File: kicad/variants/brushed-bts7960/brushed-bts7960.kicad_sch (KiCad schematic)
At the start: 57 parts, among them IC1 rp2040_RP2040_breakout_swd, J1 HDR-M-2.54_1x3, J2 HDR-M-2.54_1x4, J3 HDR-M-2.54_1x4, J4 HDR-M-2.54_1x4, U1 SN74AHC244DW, U2 BTN7970, U3 BTN7970, U4 BTN7970, U5 BTN7970, U6 BMI160, U7 SPX3819M5-L-3-3/TR

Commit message: feat(kicad): convert EasyEDA schematic to KiCad preserving wires and layout
- scripts/easyeda_sch2kicad.py: EasyEDA RP2040.json -> .kicad_sch with original component positions, wires, net labels, junctions, no-connect markers
- biba.kicad_sym: symbols regenerated from EasyEDA pin layouts (18 unique)
- ERC: 0 unconnected pins; 12 dangling wire stubs (EasyEDA polyline quirks)
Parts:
- removed C2, C3, C6: 0.1u, symbol biba:C
- removed C7: 1uF, symbol biba:C
- removed C8: 2.2uF, symbol biba:C
- removed C9: 1000uF, symbol biba:C
- removed H1, H10, H2, H3, H4, H5, H6, H7, H8: HDR-F-2.54_1x3, symbol biba:CONN_1X3
- removed IC1: rp2040_RP2040_breakout_swd, symbol biba:RP2040
- removed J1: HDR-M-2.54_1x3, symbol biba:CONN_1X3
- removed J2, J3, J4: HDR-M-2.54_1x4, symbol biba:CONN_1X4
- removed PM1: SKMW30f-05, symbol biba:SKMW30G
- removed R13, R14, R15, R16, R21, R22, R23, R24: 10k, symbol biba:R
- removed R17, R18, R19, R20, R25, R26: 1k, symbol biba:R
- removed U1: SN74AHC244DW, symbol biba:SN74AHC244
- removed U2, U3, U4, U5: BTN7970, symbol biba:BTN7970
- removed U6: BMI160, symbol biba:BMI160
- removed U7: SPX3819M5-L-3-3/TR, symbol biba:SPX3819
- added C2, C3: 0.1u, symbol biba:C_1
- added C6: 0.1u, symbol biba:C_2
- added C7: 1uF, symbol biba:C_1
- added C8: 2.2uF, symbol biba:C_2
- added C9: 1000uF, symbol biba:C_3
- added H1, H2, H3, H4, H5, H6, H7, H8: HDR-F-2.54_1x3, symbol biba:H
- added H10: HDR-F-2.54_1x3, symbol biba:H_1
- added IC1: rp2040_RP2040_breakout_swd, symbol biba:IC
- added J1: HDR-M-2.54_1x3, symbol biba:J
- added J2, J3, J4: HDR-M-2.54_1x4, symbol biba:J_1
- added PM1: SKMW30f-05, symbol biba:PM
- added R13, R16, R21, R22, R23, R24: 10k, symbol biba:R_1
- added R14, R15: 10k, symbol biba:R_2
- added R17, R18, R19, R20, R25, R26: 1k, symbol biba:R_1
- added U1: SN74AHC244DW, symbol biba:U
- added U2, U4: BTN7970, symbol biba:U_1
- added U3, U5: BTN7970, symbol biba:U_2
- added U6: BMI160, symbol biba:U_3
- added U7: SPX3819M5-L-3-3/TR, symbol biba:U_4
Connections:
- net +5V: now also C7.2, H1.2, H2.2, H3.2, H4.2, H5.2, H6.2, H7.2, H8.2, IC1.39, J1.3, J2.3, J3.1, J4.1, PM1.3, U1.20, U7.1, U7.3
- net 3.3V: now also C6.1, C8.1, R21.1, R22.2, R23.2, R24.2, U6.5, U6.8, U7.5
- net CRSF_RX: now also IC1.2, J3.4
- net CRSF_TX: now also IC1.1, J3.3
- net GND: now also C2.1, C3.1, C6.2, C7.1, C8.2, C9.2, H1.3, H10.1, H2.3, H3.3, H4.3, H5.3, H6.3, H7.3, H8.3, IC1.13, IC1.18, IC1.23, IC1.28, IC1.3, IC1.33, IC1.38, IC1.44, IC1.8, J1.1, J2.2, J2.4, J3.2, J4.2, PM1.2, PM1.5, R13.1, R14.2, R15.2, R16.1, R24.1, U1.1, U1.10, U1.19, U2.1, U3.1, U4.1, U5.1, U6.1, U6.6, U6.7, U7.2
- net GP10: now also H1.1, IC1.14
- net GP11: now also H2.1, IC1.15
- net GP14: now also H3.1, IC1.19
- net GP15: now also H4.1, IC1.20
- net GP16: now also H5.1, IC1.21
- net GP17: now also H6.1, IC1.22
- net GP18: now also H7.1, IC1.24
- net GP19: now also H8.1, IC1.25
- net I2C0_SCL: now also IC1.27, R22.1, U6.13
- net I2C0_SDA: now also IC1.26, R23.1, U6.14
- net IBAT: now also H10.3, R25.2
- net IMU_INT1: now also IC1.29, U6.4
- net IN1: now also U1.18, U2.2
- net IN2: now also U1.14, U3.2
- net IN3: now also U1.9, U4.2
- net IN4: now also U1.5, U5.2
- net INH1: now also U1.16, U2.3
- net INH2: now also U1.12, U3.3
- net INH3: now also U1.7, U4.3
- net INH4: now also U1.3, U5.3
- net L_IS: now also C3.2, IC1.32, R19.1, R20.1
- net L_LEN: now also IC1.7, U1.17
- net L_LPWM: now also IC1.5, U1.15
- net L_REN: now also IC1.6, U1.13
- net L_RPWM: now also IC1.4, U1.11
- net M1+: now also U2.4, U2.8
- net M1-: now also U3.4, U3.8
- net M2+: now also U4.4, U4.8
- net M2-: now also U5.4, U5.8
- net R_IS: now also C2.2, IC1.31, R17.1, R18.1
- net R_LEN: now also IC1.12, U1.8
- net R_LPWM: now also IC1.10, U1.6
- net R_REN: now also IC1.11, U1.4
- net R_RPWM: now also IC1.9, U1.2
- net SW: now also J2.1, PM1.6
- net UART1_RX: now also IC1.17, J4.4
- net UART1_TX: now also IC1.16, J4.3
- net VBAT: now also H10.2, R26.2
- net IC1_34: no longer names the net of C5.1
- net IC1_34: now also IC1.34, R26.1
- net IC1_35: no longer names the net of C4.1
- net IC1_35: now also IC1.35, R25.1
- net U2_5: no longer names the net of R12.2
- net U2_5: now also U2.5
- net U2_6: no longer names the net of R11.2
- net U2_6: now also R17.2, U2.6
- net U4_5: no longer names the net of R10.2
- net U4_5: now also U4.5
- net U4_6: no longer names the net of R9.2
- net U4_6: now also R19.2, U4.6
- new net: R13.2, R18.2, U3.6
- new net: R15.1, R20.2, U5.6
- new net: R21.2, U6.12
- new net: J1.2, PM1.4
- new net: R16.2, U5.5
- new net: R14.1, U3.5
- new net Vin: C9.1, PM1.1, U2.7, U3.7, U4.7, U5.7

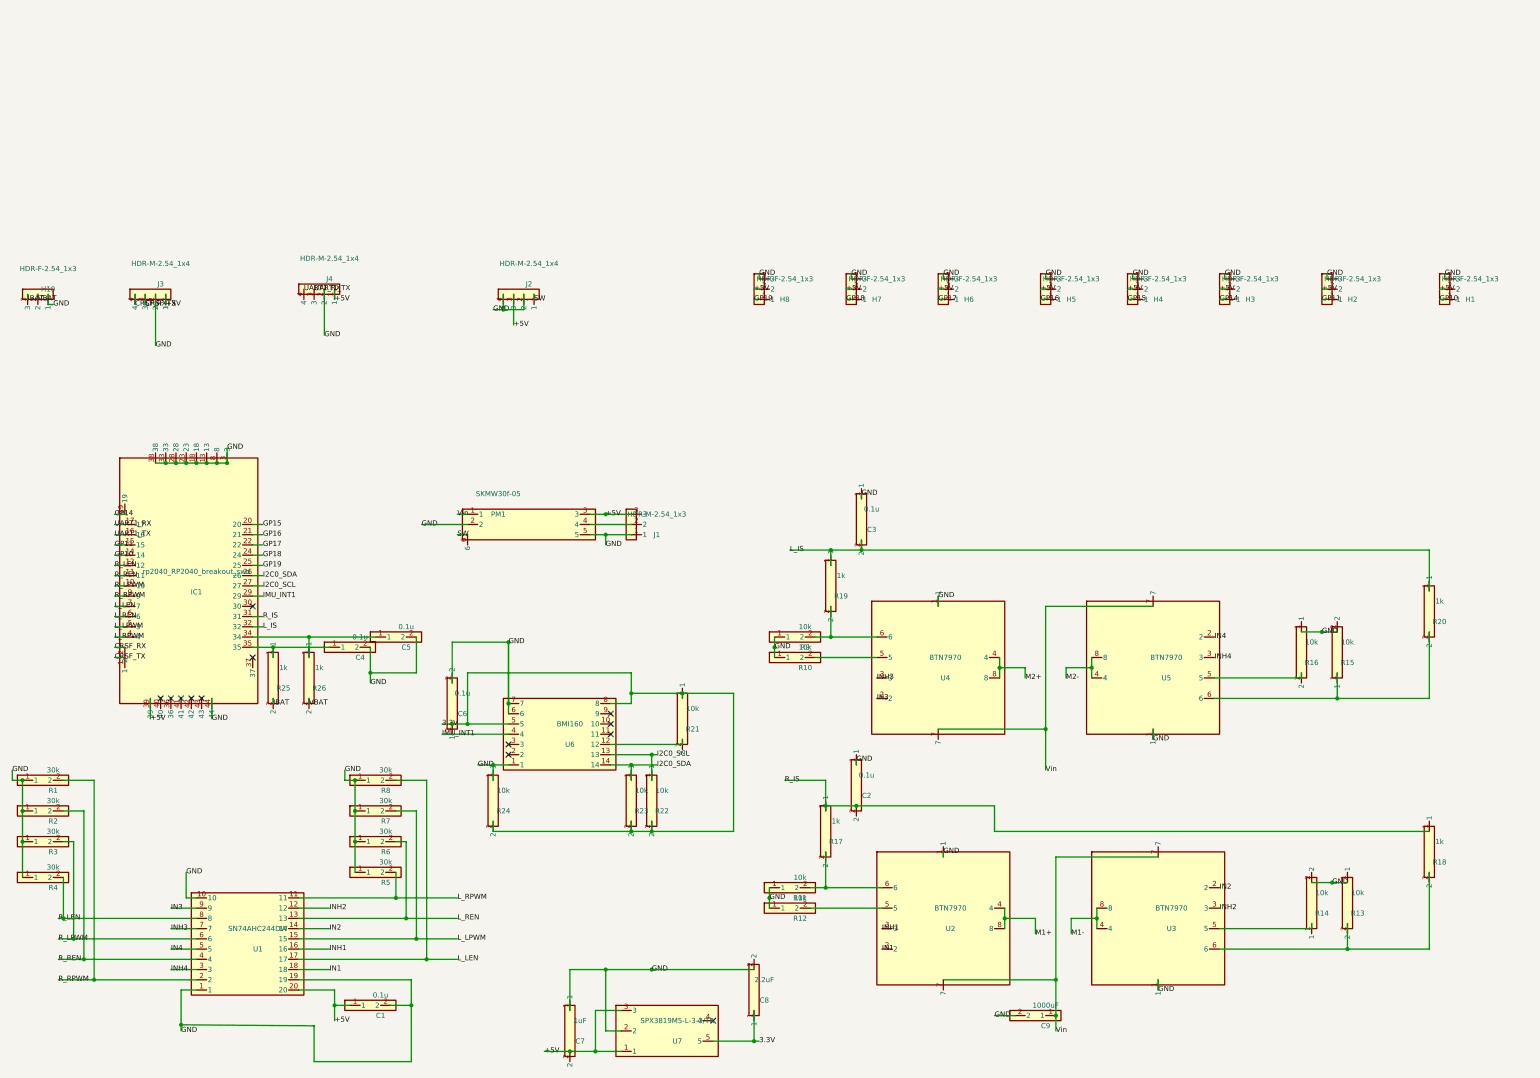
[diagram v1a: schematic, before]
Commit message: feat(kicad): preserve full EasyEDA symbol graphics and pin geometry
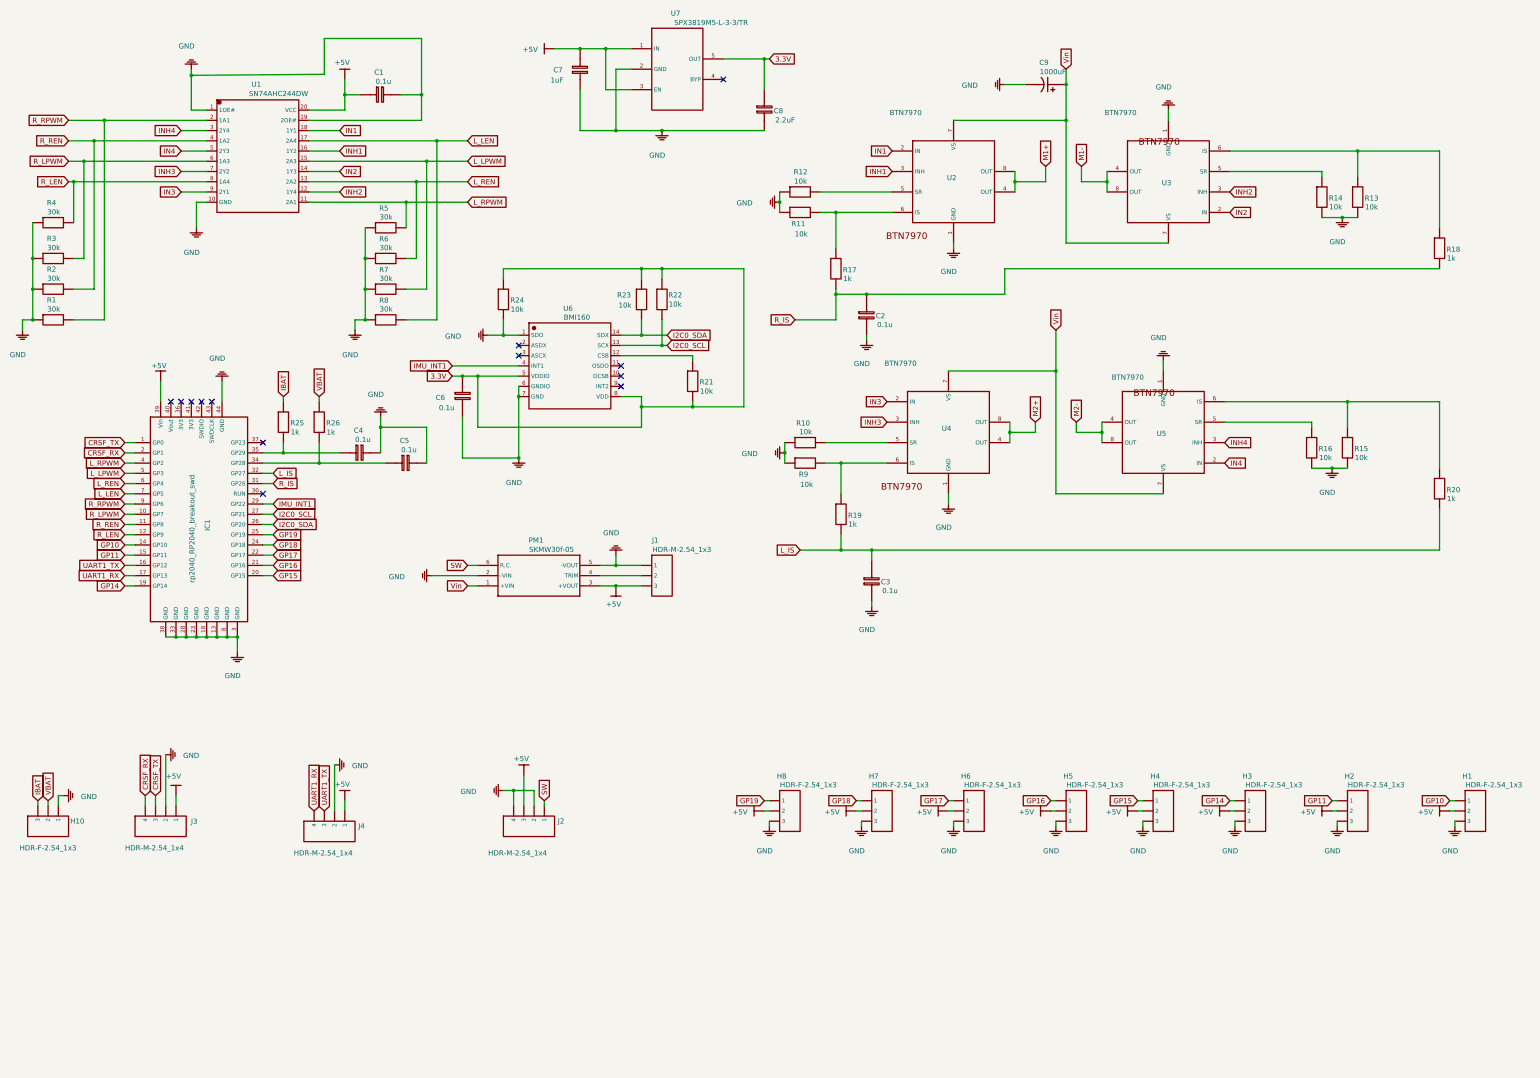
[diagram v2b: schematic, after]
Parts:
- removed C9: 1000uF, symbol biba:C_3
- removed H1, H2, H3, H4, H5, H6, H7, H8: HDR-F-2.54_1x3, symbol biba:H
- removed H10: HDR-F-2.54_1x3, symbol biba:H_1
- removed IC1: rp2040_RP2040_breakout_swd, symbol biba:IC
- removed J1: HDR-M-2.54_1x3, symbol biba:J
- removed J2, J3, J4: HDR-M-2.54_1x4, symbol biba:J_1
- removed PM1: SKMW30f-05, symbol biba:PM
- removed U1: SN74AHC244DW, symbol biba:U
- removed U2, U4: BTN7970, symbol biba:U_1
- removed U3, U5: BTN7970, symbol biba:U_2
- removed U6: BMI160, symbol biba:U_3
- removed U7: SPX3819M5-L-3-3/TR, symbol biba:U_4
- added C9: 1000uF, symbol biba:C_Pol
- added H1, H2, H3, H4, H5, H6, H7, H8: HDR-F-2.54_1x3, symbol biba:HDR-F-2.54_1x3
- added H10: HDR-F-2.54_1x3, symbol biba:HDR-F-2.54_1x3_1
- added IC1: rp2040_RP2040_breakout_swd, symbol biba:rp2040_RP2040_breakout_swd
- added J1: HDR-M-2.54_1x3, symbol biba:HDR-M-2.54_1x3
- added J2, J3, J4: HDR-M-2.54_1x4, symbol biba:HDR-M-2.54_1x4
- added PM1: SKMW30f-05, symbol biba:SKMW30f-05
- added U1: SN74AHC244DW, symbol biba:SN74AHC244DW
- added U2, U4: BTN7970, symbol biba:BTN7970
- added U3: BTN7970, symbol biba:BTN7970_1
- added U5: BTN7970, symbol biba:BTN7970_2
- added U6: BMI160, symbol biba:BMI160
- added U7: SPX3819M5-L-3-3/TR, symbol biba:SPX3819M5-L-3-3_TR
- C1, C2, C3, C4, C5, C6: Package (none) -> C0805
- C7, C8: Package (none) -> C0603
- R1, R10, R11, R12, R13, R14, R15, R16, R17, R18, R19, R2, R20, R25, R26, R3, R4, R5, R6, R7, R8, R9: Package (none) -> R0805
- R21, R22, R23, R24: Package (none) -> R0603
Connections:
- net +5V: now also H1.2, H2.2, H3.2, H4.2, H5.2, H6.2, H7.2, H8.2, IC1.39 (Vin), J1.3, J2.3, J3.1, J4.1, PM1.3 (+VOUT), U1.20 (VCC), U7.1 (IN), U7.3 (EN)
- net 3.3V: now also U6.5 (VDDIO), U6.8 (VDD), U7.5 (OUT)
- net CRSF_RX: now also IC1.2 (GP1), J3.4
- net CRSF_TX: now also IC1.1 (GP0), J3.3
- net GND: now also C9.2, H1.3, H10.1, H2.3, H3.3, H4.3, H5.3, H6.3, H7.3, H8.3, IC1.13 (GND), IC1.18 (GND), IC1.23 (GND), IC1.28 (GND), IC1.3 (GND), IC1.33 (GND), IC1.38 (GND), IC1.44 (GND), IC1.8 (GND), J1.1, J2.2, J2.4, J3.2, J4.2, PM1.2 (-VIN), PM1.5 (-VOUT), U1.1 (1OE#), U1.10 (GND), U1.19 (2OE#), U2.1 (GND), U3.1 (GND), U4.1 (GND), U5.1 (GND), U6.1 (SDO), U6.6 (GNDIO), U6.7 (GND), U7.2 (GND)
- net GP10: now also H1.1, IC1.14 (GP10)
- net GP11: now also H2.1, IC1.15 (GP11)
- net GP14: now also H3.1, IC1.19 (GP14)
- net GP15: now also H4.1, IC1.20 (GP15)
- net GP16: now also H5.1, IC1.21 (GP16)
- net GP17: now also H6.1, IC1.22 (GP17)
- net GP18: now also H7.1, IC1.24 (GP18)
- net GP19: now also H8.1, IC1.25 (GP19)
- net I2C0_SCL: now also IC1.27 (GP21), U6.13 (SCX)
- net I2C0_SDA: now also IC1.26 (GP20), U6.14 (SDX)
- net IBAT: now also H10.3
- net IMU_INT1: now also IC1.29 (GP22), U6.4 (INT1)
- net IN1: now also U1.18 (1Y1), U2.2 (IN)
- net IN2: now also U1.14 (1Y3), U3.2 (IN)
- net IN3: now also U1.9 (2Y1), U4.2 (IN)
- net IN4: now also U1.5 (2Y3), U5.2 (IN)
- net INH1: now also U1.16 (1Y2), U2.3 (INH)
- net INH2: now also U1.12 (1Y4), U3.3 (INH)
- net INH3: now also U1.7 (2Y2), U4.3 (INH)
- net INH4: now also U1.3 (2Y4), U5.3 (INH)
- net L_IS: now also IC1.32 (GP27)
- net L_LEN: now also IC1.7 (GP5), U1.17 (2A4)
- net L_LPWM: now also IC1.5 (GP3), U1.15 (2A3)
- net L_REN: now also IC1.6 (GP4), U1.13 (2A2)
- net L_RPWM: now also IC1.4 (GP2), U1.11 (2A1)
- net M1+: now also U2.4 (OUT), U2.8 (OUT)
- net M1-: now also U3.4 (OUT), U3.8 (OUT)
- net M2+: now also U4.4 (OUT), U4.8 (OUT)
- net M2-: now also U5.4 (OUT), U5.8 (OUT)
- net R_IS: now also IC1.31 (GP26)
- net R_LEN: now also IC1.12 (GP9), U1.8 (1A4)
- net R_LPWM: now also IC1.10 (GP7), U1.6 (1A3)
- net R_REN: now also IC1.11 (GP8), U1.4 (1A2)
- net R_RPWM: now also IC1.9 (GP6), U1.2 (1A1)
- net SW: now also J2.1, PM1.6 (R.C.)
- net UART1_RX: now also IC1.17 (GP13), J4.4
- net UART1_TX: now also IC1.16 (GP12), J4.3
- net VBAT: now also H10.2
- net Vin: now also C9.1, PM1.1 (+VIN), U2.7 (VS), U3.7 (VS), U4.7 (VS), U5.7 (VS)
- net at C5.1, R26.1: now also IC1.34 (GP28)
- net at C4.1, R25.1: now also IC1.35 (GP29)
- net at R10.2: now also U4.5 (SR)
- net at R13.2, R18.2: now also U3.6 (IS)
- net at R15.1, R20.2: now also U5.6 (IS)
- net at R11.2, R17.2: now also U2.6 (IS)
- net at R21.2: now also U6.12 (CSB)
- net at R19.2, R9.2: now also U4.6 (IS)
- net at R12.2: now also U2.5 (SR)
- net at R16.2: now also U5.5 (SR)
- net at R14.1: now also U3.5 (SR)
- new net: J1.2, PM1.4 (TRIM)
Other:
- title: (none) -> BiBa — RP2040, 4× BTN7970 (brushed)

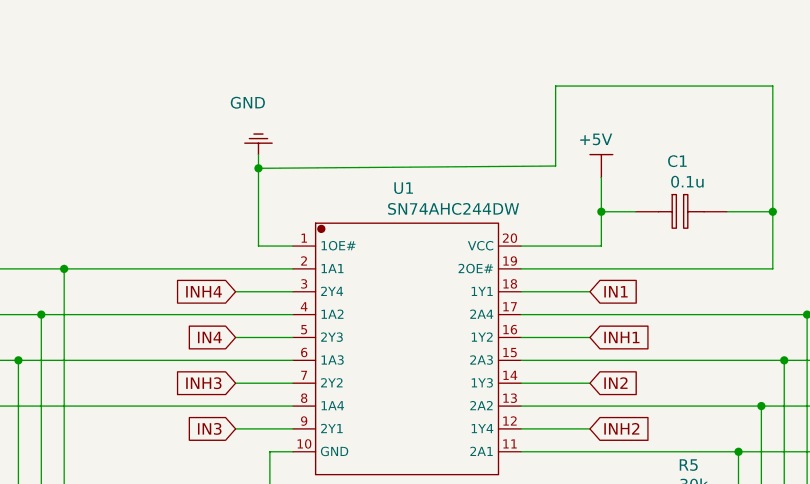
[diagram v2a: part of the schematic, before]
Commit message: fix(kicad): snap wire/junction points to grid and regenerate project file
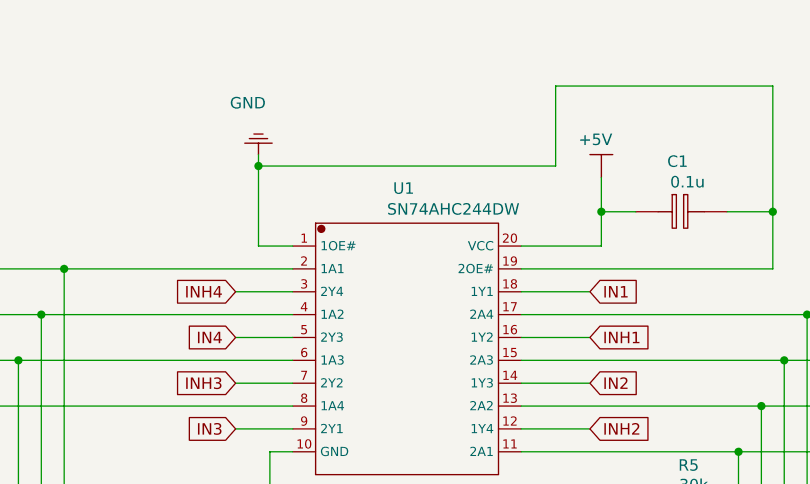
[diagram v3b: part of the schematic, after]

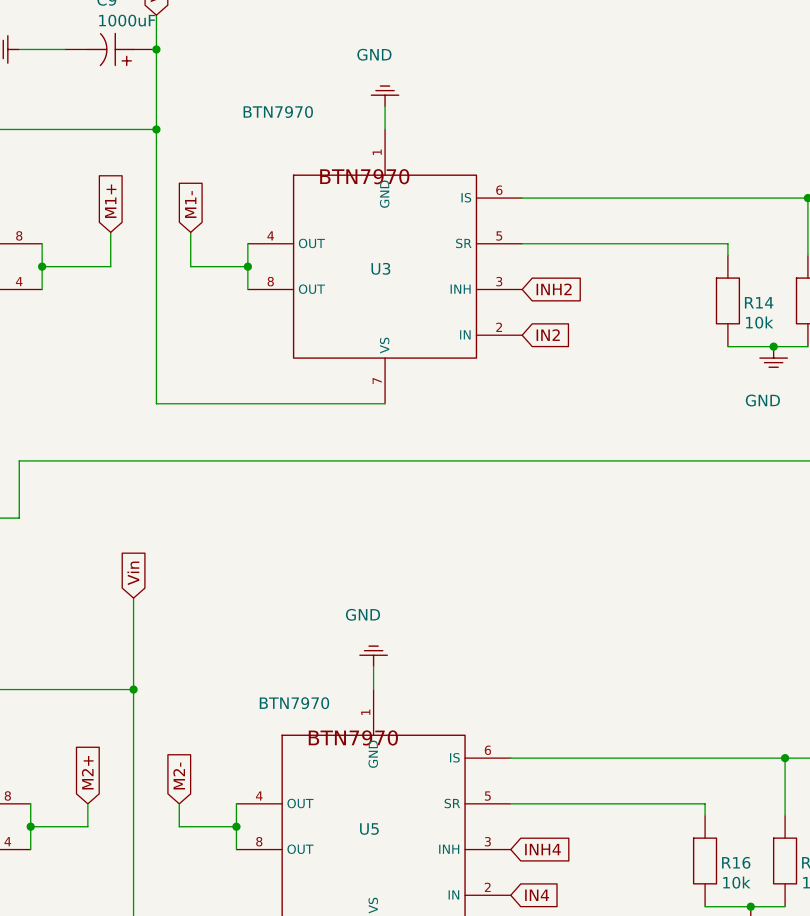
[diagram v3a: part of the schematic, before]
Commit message: fix(kicad): regenerate variant with stable UUIDs and correct text justification
- switch to deterministic UUIDv5 so regeneration yields minimal diffs
- map flipped text anchors to right justify and align sheet UUIDs across files
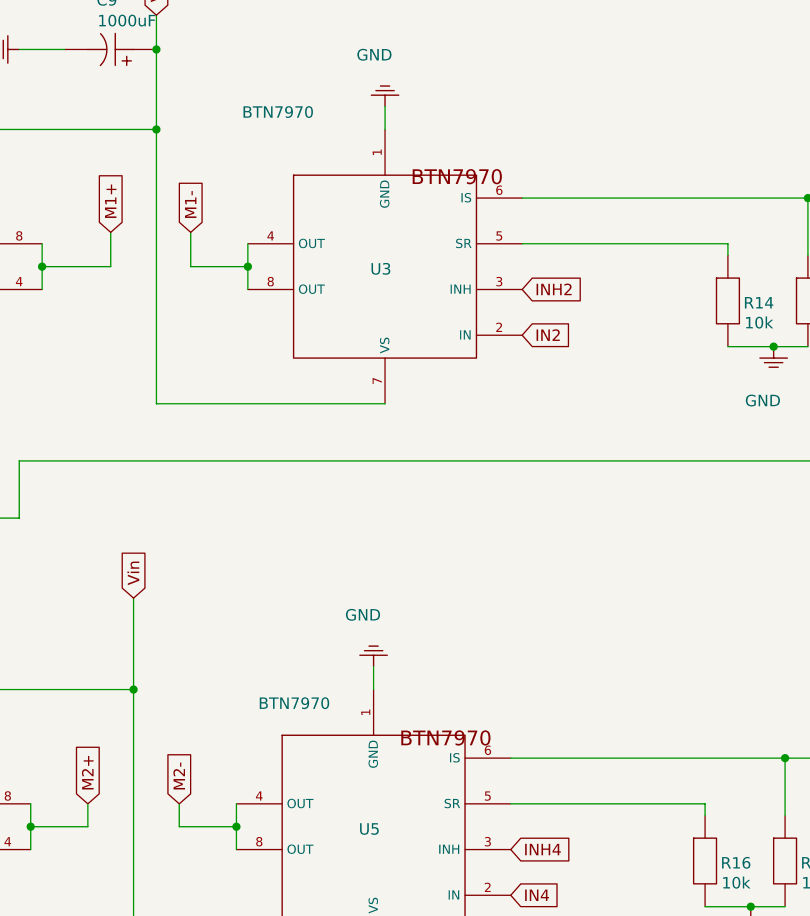
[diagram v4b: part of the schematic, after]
